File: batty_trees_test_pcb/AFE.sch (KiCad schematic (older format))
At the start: 0 parts

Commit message: Finished off Power section and made up AFE schematic
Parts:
- added D? (x8): B240A-13-F, digikey-footprints:DO-214AC, symbol dk_Diodes-Rectifiers-Single:B240A-13-F
- added J? (x2): JSH_PH_B3B-PH-K, Connector_JST:JST_PH_B3B-PH-K_1x03_P2.00mm_Vertical, symbol Connector:Conn_01x03_Male
- added J? (x2): Header, Connector_PinHeader_2.54mm:PinHeader_1x03_P2.54mm_Vertical, symbol Connector:Conn_01x03_Male
- added JP? (x2): Jumper, Connector_PinHeader_2.54mm:PinHeader_1x02_P2.54mm_Vertical, symbol Device:Jumper_NO_Small
- added R? (x8): 10k, Resistor_SMD:R_0805_2012Metric_Pad1.15x1.40mm_HandSolder, symbol Device:R
- added R? (x8): 100k, Resistor_SMD:R_0805_2012Metric_Pad1.15x1.40mm_HandSolder, symbol Device:R
- added R? (x8): 33k, Resistor_SMD:R_0805_2012Metric_Pad1.15x1.40mm_HandSolder, symbol Device:R
- added R? (x4): 0, Resistor_SMD:R_0805_2012Metric_Pad1.15x1.40mm_HandSolder, symbol Device:R
- added R? (x8): 1k, Resistor_SMD:R_0805_2012Metric_Pad1.15x1.40mm_HandSolder, symbol Device:R
- added R? (x2): 330, Resistor_SMD:R_0805_2012Metric_Pad1.15x1.40mm_HandSolder, symbol Device:R
- added TP? (x6): Test Point, OSU_SIM_BASIC:Keystone_5019, symbol Connector:TestPoint_Alt
- added U? (x12): LMH6611, Package_TO_SOT_SMD:TSOT-23-6, symbol Amplifier_Operational:LMH6611
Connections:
- new net: D?.A, D?.K, R?.1, U?.3 (+) (x4)
- new net: J?.1 (Pin_1), R?.2 (x2)
- new net: J?.3 (Pin_3), R?.2 (x2)
- new net: R?.1, R?.1, U?.3 (+) (x4)
- new net: R?.1, R?.1, U?.4 (-) (x4)
- new net: R?.2, R?.2, R?.2, U?.1 (x4)
- new net: JP?.1, R?.1, TP?.1, U?.1 (x2)
- new net: R?.1, R?.2, R?.2, U?.4 (-) (x2)
- new net: R?.1, R?.1, U?.1 (x2)
- new net: R?.1, R?.2, U?.4 (-) (x2)
- new net +3V3: D?.K, D?.K, D?.K, D?.K, U?.5 (~DISABLE), U?.5 (~DISABLE), U?.5 (~DISABLE), U?.5 (~DISABLE), U?.5 (~DISABLE), U?.5 (~DISABLE), U?.5 (~DISABLE), U?.5 (~DISABLE), U?.5 (~DISABLE), U?.5 (~DISABLE), U?.5 (~DISABLE), U?.5 (~DISABLE), U?.6 (V+), U?.6 (V+), U?.6 (V+), U?.6 (V+), U?.6 (V+), U?.6 (V+), U?.6 (V+), U?.6 (V+), U?.6 (V+), U?.6 (V+), U?.6 (V+), U?.6 (V+)
- new net GND: D?.A, D?.A, D?.A, D?.A, J?.2 (Pin_2), J?.2 (Pin_2), J?.2 (Pin_2), J?.2 (Pin_2), R?.2, R?.2, R?.2, R?.2, U?.2 (V-), U?.2 (V-), U?.2 (V-), U?.2 (V-), U?.2 (V-), U?.2 (V-), U?.2 (V-), U?.2 (V-), U?.2 (V-), U?.2 (V-), U?.2 (V-), U?.2 (V-)
- new net L_VIN_BUFN: J?.3 (Pin_3), R?.1, R?.2, R?.2, U?.1, U?.4 (-)
- new net L_VIN_BUFP: J?.1 (Pin_1), R?.1, R?.2, R?.2, U?.1, U?.4 (-)
- new net R_VIN_BUFN: J?.3 (Pin_3), R?.1, R?.2, R?.2, U?.1, U?.4 (-)
- new net R_VIN_BUFP: J?.1 (Pin_1), R?.1, R?.2, R?.2, U?.1, U?.4 (-)
- new net VMID: R?.2, R?.2, R?.2, R?.2, U?.3 (+), U?.3 (+), U?.3 (+), U?.3 (+)
- new net dd_lin: JP?.2
- new net dd_rin: JP?.2
- new net l_vinn: R?.1, TP?.1
- new net l_vinp: R?.1, TP?.1
- new net r_vinn: R?.1, TP?.1
- new net r_vinp: R?.1, TP?.1
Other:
- note added: "Diff to single ended converter \nwith level shift and gain reduction\nVmid level shift 1/3 gain reduction"
- note added: "Left and right Contact mic input circuitry.\nInpnut clamped at 3.3 and the second stage has gain of\n1/3 to reduce the max input range to 1.2V centered around VMID\nFirst stage buffesrs input with high input impeadance and second stage\nlevel shifts and reduces the gain of the input signal"

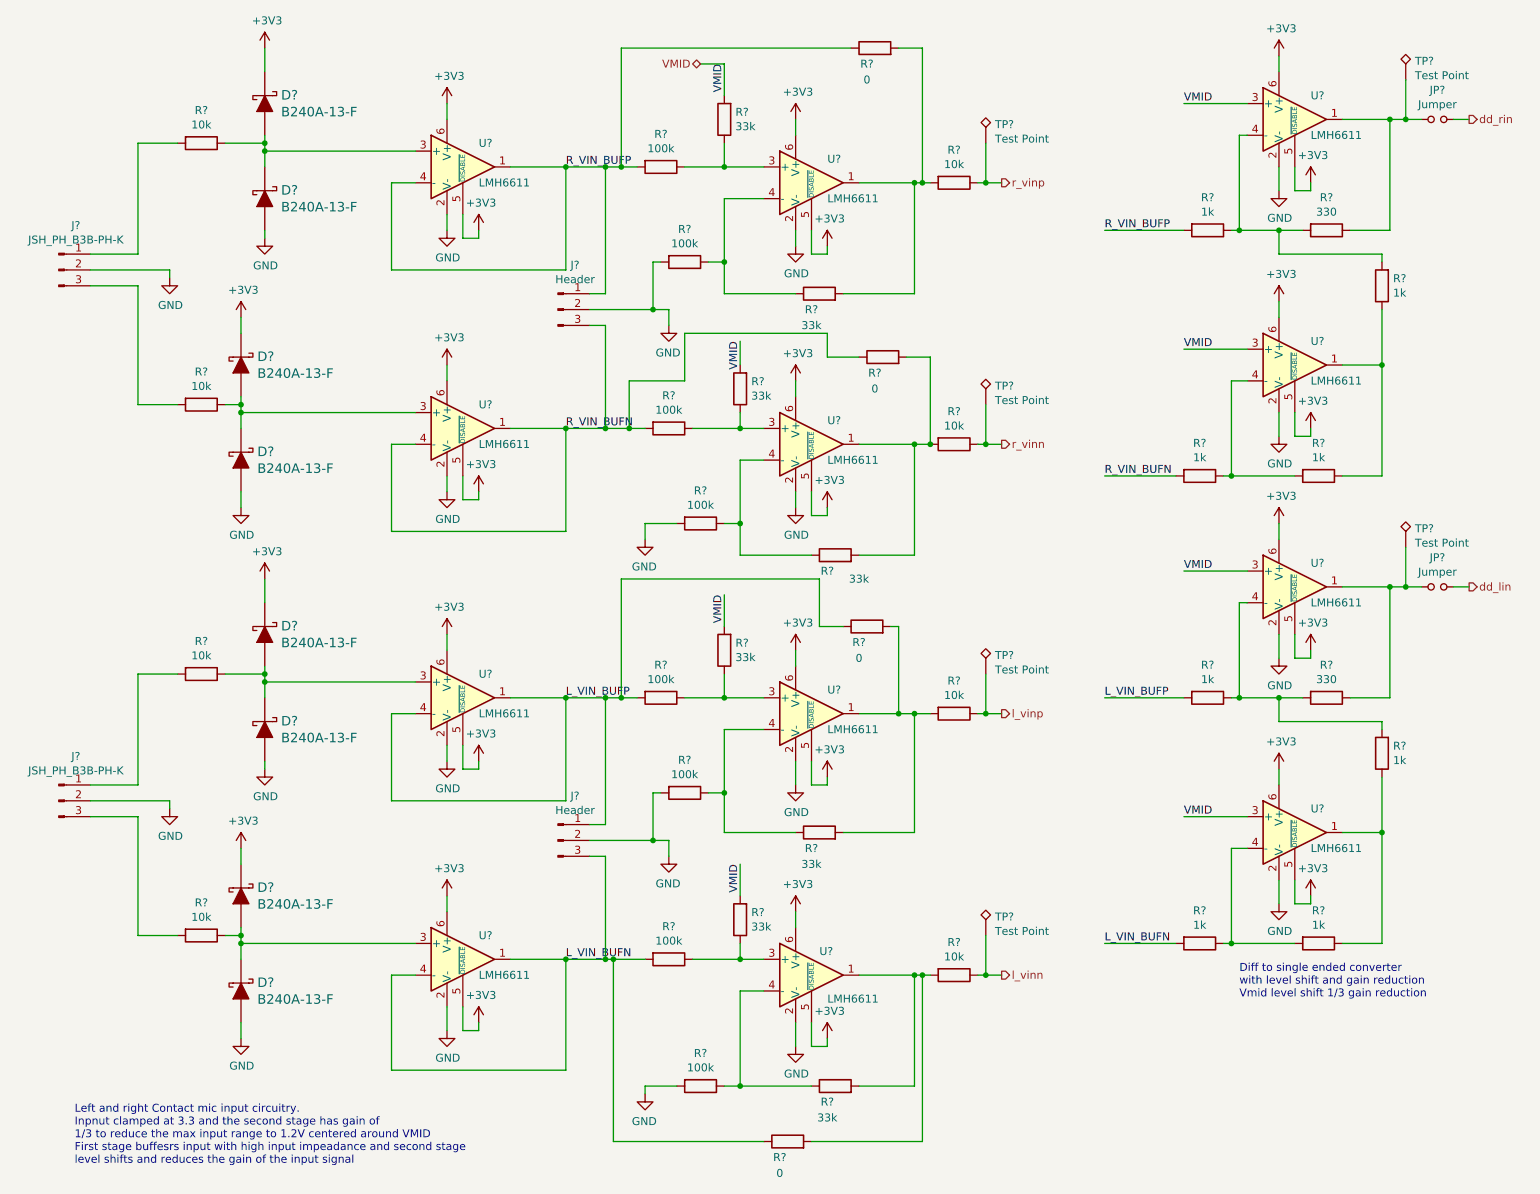
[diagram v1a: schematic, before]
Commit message: wired up chip to fpga on schematic and begininng to do layout
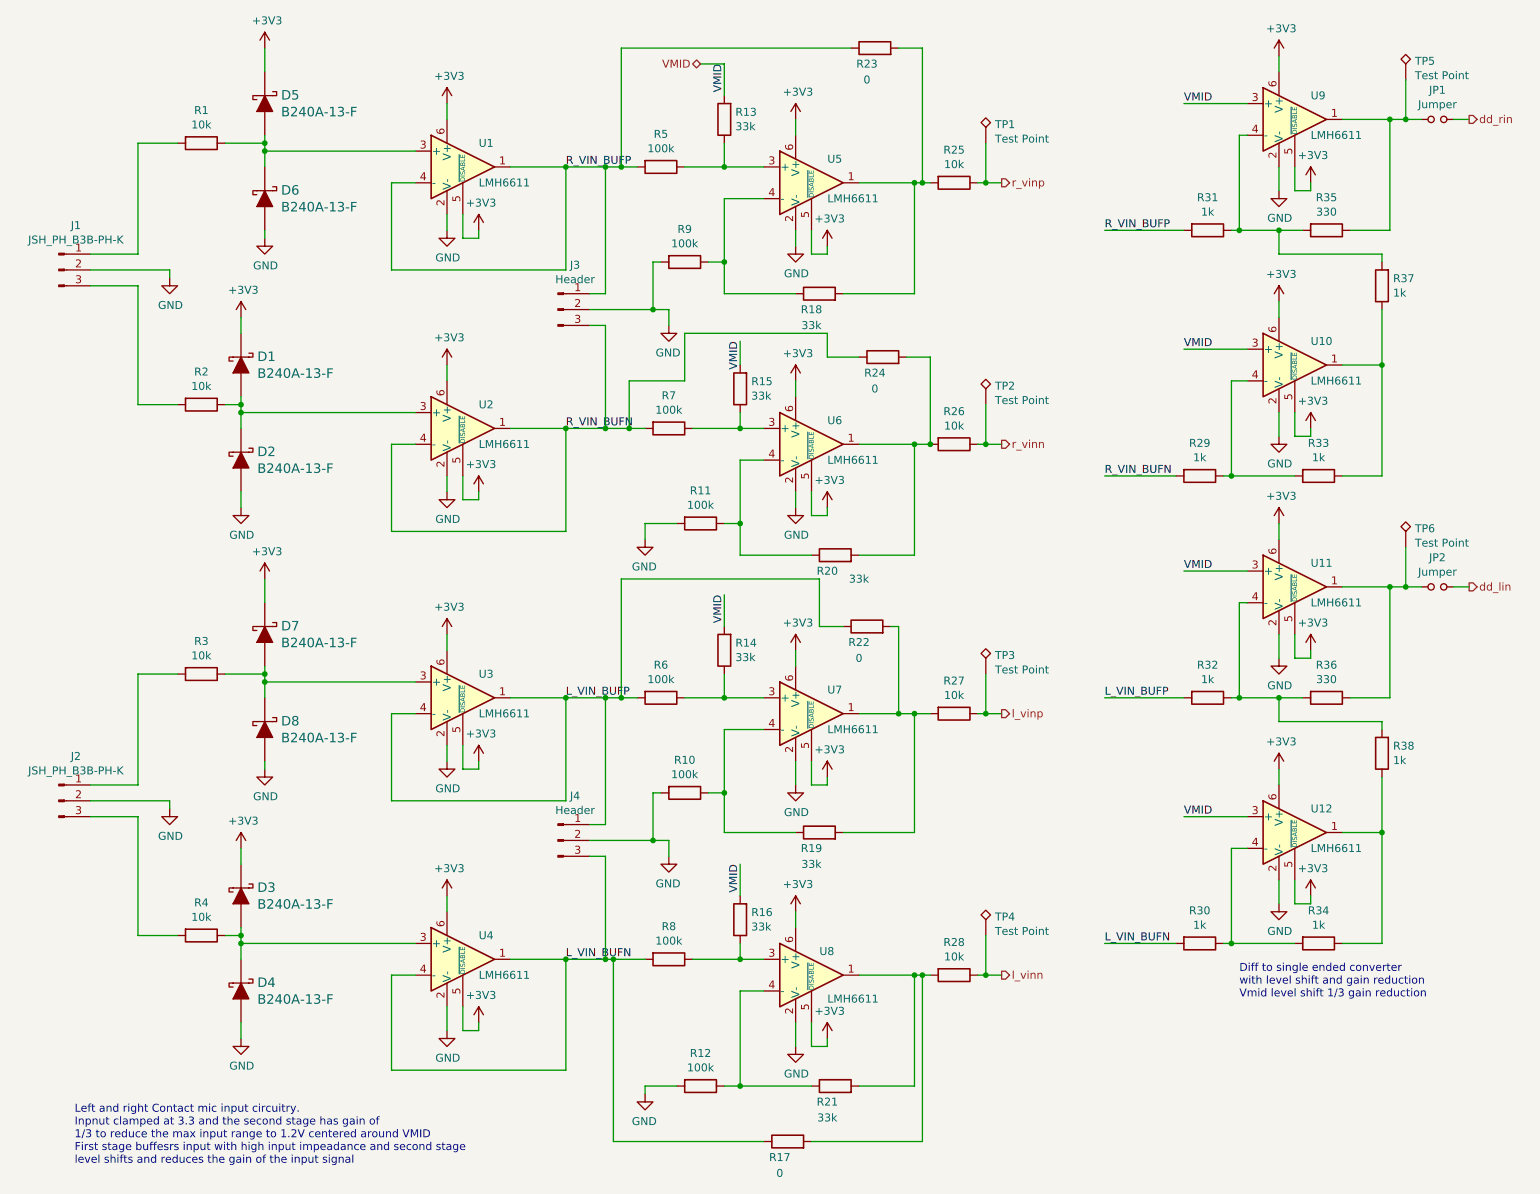
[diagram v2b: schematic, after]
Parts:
- gave numbers to parts that had none: 70

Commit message: more layout work ~90% finished
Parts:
- added C23, C24, C25, C26, C27, C28, C29, C30, C31, C32, C33, C34: 0.1uF, Capacitor_SMD:C_0805_2012Metric_Pad1.15x1.40mm_HandSolder, symbol Device:C_Small
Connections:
- net +3V3: now also C23.1, C24.1, C25.1, C26.1, C27.1, C28.1, C29.1, C30.1, C31.1, C32.1, C33.1, C34.1
- net GND: now also C23.2, C24.2, C25.2, C26.2, C27.2, C28.2, C29.2, C30.2, C31.2, C32.2, C33.2, C34.2
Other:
- note added: "Decap 1 per package"

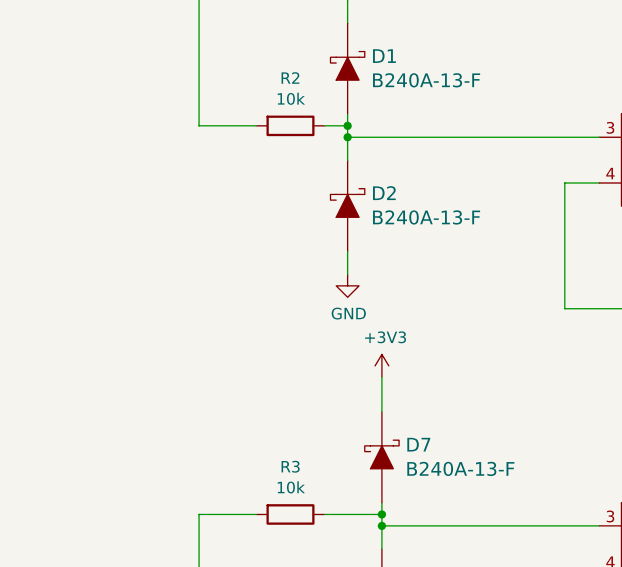
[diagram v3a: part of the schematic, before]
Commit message: all componenets updated with digikey pn bom generated
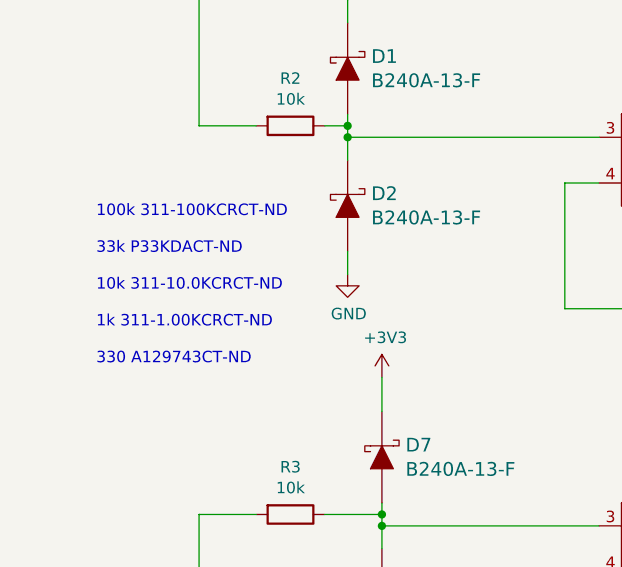
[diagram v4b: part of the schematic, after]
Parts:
- R1, R2, R25, R26, R27, R28, R3, R4: Digi-Key_PN (none) -> 311-10.0KCRCT
- R10, R11, R12, R5, R6, R7, R8, R9: Digi-Key_PN (none) -> 311-100KCRCT-ND
- R13, R14, R15, R16, R18, R19, R20, R21: Digi-Key_PN (none) -> P33KDACT-ND
- R29, R30, R31, R32, R33, R34, R37, R38: Digi-Key_PN (none) -> 311-1.00KCRCT-ND
- R35, R36: Digi-Key_PN (none) -> A129743CT-ND
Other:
- note added: "100k 311-100KCRCT-ND\n\n33k P33KDACT-ND\n\n10k 311-10.0KCRCT-ND\n\n1k 311-1.00KCRCT-ND\n\n330 A129743CT-ND"
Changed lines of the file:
@@
 F 2 "Resistor_SMD:R_0805_2012Metric_Pad1.15x1.40mm_HandSolder" V 1580 1300 50  0001 C CNN
 F 3 "~" H 1650 1300 50  0001 C CNN
+F 4 "311-10.0KCRCT" V 1650 1300 50  0001 C CNN "Digi-Key_PN"
 	1    1650 1300
 	0    1    1    0
@@
 F 2 "Resistor_SMD:R_0805_2012Metric_Pad1.15x1.40mm_HandSolder" V 1580 2950 50  0001 C CNN
 F 3 "~" H 1650 2950 50  0001 C CNN
+F 4 "311-10.0KCRCT" V 1650 2950 50  0001 C CNN "Digi-Key_PN"
 	1    1650 2950
 	0    1    1    0
@@
 F 2 "Resistor_SMD:R_0805_2012Metric_Pad1.15x1.40mm_HandSolder" V 4480 1450 50  0001 C CNN
 F 3 "~" H 4550 1450 50  0001 C CNN
+F 4 "311-100KCRCT-ND" V 4550 1450 50  0001 C CNN "Digi-Key_PN"
 	1    4550 1450
 	0    1    1    0
@@
 F 2 "Resistor_SMD:R_0805_2012Metric_Pad1.15x1.40mm_HandSolder" V 4880 1150 50  0001 C CNN
 F 3 "~" H 4950 1150 50  0001 C CNN
+F 4 "P33KDACT-ND" H 4950 1150 50  0001 C CNN "Digi-Key_PN"
 	1    4950 1150
 	-1   0    0    1
@@
 F 2 "Resistor_SMD:R_0805_2012Metric_Pad1.15x1.40mm_HandSolder" V 4530 3100 50  0001 C CNN
 F 3 "~" H 4600 3100 50  0001 C CNN
+F 4 "311-100KCRCT-ND" V 4600 3100 50  0001 C CNN "Digi-Key_PN"
 	1    4600 3100
 	0    1    1    0
@@
 F 2 "Resistor_SMD:R_0805_2012Metric_Pad1.15x1.40mm_HandSolder" V 4980 2850 50  0001 C CNN
 F 3 "~" H 5050 2850 50  0001 C CNN
+F 4 "P33KDACT-ND" H 5050 2850 50  0001 C CNN "Digi-Key_PN"
 	1    5050 2850
 	-1   0    0    1
@@
 F 2 "Resistor_SMD:R_0805_2012Metric_Pad1.15x1.40mm_HandSolder" V 5480 2250 50  0001 C CNN
 F 3 "~" H 5550 2250 50  0001 C CNN
+F 4 "P33KDACT-ND" V 5550 2250 50  0001 C CNN "Digi-Key_PN"
 	1    5550 2250
 	0    -1   -1   0
@@
 F 2 "Resistor_SMD:R_0805_2012Metric_Pad1.15x1.40mm_HandSolder" V 4630 2050 50  0001 C CNN
 F 3 "~" H 4700 2050 50  0001 C CNN
+F 4 "311-100KCRCT-ND" V 4700 2050 50  0001 C CNN "Digi-Key_PN"
 	1    4700 2050
 	0    1    1    0
@@
 F 2 "Resistor_SMD:R_0805_2012Metric_Pad1.15x1.40mm_HandSolder" V 5580 3900 50  0001 C CNN
 F 3 "~" H 5650 3900 50  0001 C CNN
+F 4 "P33KDACT-ND" V 5650 3900 50  0001 C CNN "Digi-Key_PN"
 	1    5650 3900
 	0    -1   -1   0
@@
 F 2 "Resistor_SMD:R_0805_2012Metric_Pad1.15x1.40mm_HandSolder" V 4730 3700 50  0001 C CNN
 F 3 "~" H 4800 3700 50  0001 C CNN
+F 4 "311-100KCRCT-ND" V 4800 3700 50  0001 C CNN "Digi-Key_PN"
 	1    4800 3700
 	0    1    1    0
@@
 F 2 "Resistor_SMD:R_0805_2012Metric_Pad1.15x1.40mm_HandSolder" V 6330 3200 50  0001 C CNN
 F 3 "~" H 6400 3200 50  0001 C CNN
+F 4 "311-10.0KCRCT" V 6400 3200 50  0001 C CNN "Digi-Key_PN"
 	1    6400 3200
 	0    1    1    0
@@
 F 2 "Resistor_SMD:R_0805_2012Metric_Pad1.15x1.40mm_HandSolder" V 6330 1550 50  0001 C CNN
 F 3 "~" H 6400 1550 50  0001 C CNN
+F 4 "311-10.0KCRCT" V 6400 1550 50  0001 C CNN "Digi-Key_PN"
 	1    6400 1550
 	0    1    1    0
@@
 F 2 "Resistor_SMD:R_0805_2012Metric_Pad1.15x1.40mm_HandSolder" V 1580 4650 50  0001 C CNN
 F 3 "~" H 1650 4650 50  0001 C CNN
+F 4 "311-10.0KCRCT" V 1650 4650 50  0001 C CNN "Digi-Key_PN"
 	1    1650 4650
 	0    1    1    0
@@
 F 2 "Resistor_SMD:R_0805_2012Metric_Pad1.15x1.40mm_HandSolder" V 1580 6300 50  0001 C CNN
 F 3 "~" H 1650 6300 50  0001 C CNN
+F 4 "311-10.0KCRCT" V 1650 6300 50  0001 C CNN "Digi-Key_PN"
 	1    1650 6300
 	0    1    1    0
@@
 F 2 "Resistor_SMD:R_0805_2012Metric_Pad1.15x1.40mm_HandSolder" V 4480 4800 50  0001 C CNN
 F 3 "~" H 4550 4800 50  0001 C CNN
+F 4 "311-100KCRCT-ND" V 4550 4800 50  0001 C CNN "Digi-Key_PN"
 	1    4550 4800
 	0    1    1    0
@@
 F 2 "Resistor_SMD:R_0805_2012Metric_Pad1.15x1.40mm_HandSolder" V 4880 4500 50  0001 C CNN
 F 3 "~" H 4950 4500 50  0001 C CNN
+F 4 "P33KDACT-ND" H 4950 4500 50  0001 C CNN "Digi-Key_PN"
 	1    4950 4500
 	-1   0    0    1
@@
 F 2 "Resistor_SMD:R_0805_2012Metric_Pad1.15x1.40mm_HandSolder" V 4530 6450 50  0001 C CNN
 F 3 "~" H 4600 6450 50  0001 C CNN
+F 4 "311-100KCRCT-ND" V 4600 6450 50  0001 C CNN "Digi-Key_PN"
 	1    4600 6450
 	0    1    1    0
@@
 F 2 "Resistor_SMD:R_0805_2012Metric_Pad1.15x1.40mm_HandSolder" V 4980 6200 50  0001 C CNN
 F 3 "~" H 5050 6200 50  0001 C CNN
+F 4 "P33KDACT-ND" H 5050 6200 50  0001 C CNN "Digi-Key_PN"
 	1    5050 6200
 	-1   0    0    1
@@
 F 2 "Resistor_SMD:R_0805_2012Metric_Pad1.15x1.40mm_HandSolder" V 5480 5650 50  0001 C CNN
 F 3 "~" H 5550 5650 50  0001 C CNN
+F 4 "P33KDACT-ND" V 5550 5650 50  0001 C CNN "Digi-Key_PN"
 	1    5550 5650
 	0    -1   -1   0
@@
 F 2 "Resistor_SMD:R_0805_2012Metric_Pad1.15x1.40mm_HandSolder" V 4630 5400 50  0001 C CNN
 F 3 "~" H 4700 5400 50  0001 C CNN
+F 4 "311-100KCRCT-ND" V 4700 5400 50  0001 C CNN "Digi-Key_PN"
 	1    4700 5400
 	0    1    1    0
@@
 F 2 "Resistor_SMD:R_0805_2012Metric_Pad1.15x1.40mm_HandSolder" V 5580 7250 50  0001 C CNN
 F 3 "~" H 5650 7250 50  0001 C CNN
+F 4 "P33KDACT-ND" V 5650 7250 50  0001 C CNN "Digi-Key_PN"
 	1    5650 7250
 	0    -1   -1   0
@@
 F 2 "Resistor_SMD:R_0805_2012Metric_Pad1.15x1.40mm_HandSolder" V 4730 7250 50  0001 C CNN
 F 3 "~" H 4800 7250 50  0001 C CNN
+F 4 "311-100KCRCT-ND" V 4800 7250 50  0001 C CNN "Digi-Key_PN"
 	1    4800 7250
 	0    1    1    0
@@
 F 2 "Resistor_SMD:R_0805_2012Metric_Pad1.15x1.40mm_HandSolder" V 6330 6550 50  0001 C CNN
 F 3 "~" H 6400 6550 50  0001 C CNN
+F 4 "311-10.0KCRCT" V 6400 6550 50  0001 C CNN "Digi-Key_PN"
 	1    6400 6550
 	0    1    1    0
@@
 F 2 "Resistor_SMD:R_0805_2012Metric_Pad1.15x1.40mm_HandSolder" V 6330 4900 50  0001 C CNN
 F 3 "~" H 6400 4900 50  0001 C CNN
+F 4 "311-10.0KCRCT" V 6400 4900 50  0001 C CNN "Digi-Key_PN"
 	1    6400 4900
 	0    1    1    0
@@
 F 2 "Resistor_SMD:R_0805_2012Metric_Pad1.15x1.40mm_HandSolder" V 8630 3400 50  0001 C CNN
 F 3 "~" H 8700 3400 50  0001 C CNN
+F 4 "311-1.00KCRCT-ND" V 8700 3400 50  0001 C CNN "Digi-Key_PN"
 	1    8700 3400
 	0    1    1    0
@@
 F 2 "Resistor_SMD:R_0805_2012Metric_Pad1.15x1.40mm_HandSolder" V 7880 3400 50  0001 C CNN
 F 3 "~" H 7950 3400 50  0001 C CNN
+F 4 "311-1.00KCRCT-ND" V 7950 3400 50  0001 C CNN "Digi-Key_PN"
 	1    7950 3400
 	0    1    1    0
@@
 F 2 "Resistor_SMD:R_0805_2012Metric_Pad1.15x1.40mm_HandSolder" V 9030 2200 50  0001 C CNN
 F 3 "~" H 9100 2200 50  0001 C CNN
+F 4 "311-1.00KCRCT-ND" H 9100 2200 50  0001 C CNN "Digi-Key_PN"
 	1    9100 2200
 	-1   0    0    1
@@
 F 2 "Resistor_SMD:R_0805_2012Metric_Pad1.15x1.40mm_HandSolder" V 8680 1850 50  0001 C CNN
 F 3 "~" H 8750 1850 50  0001 C CNN
+F 4 "A129743CT-ND" V 8750 1850 50  0001 C CNN "Digi-Key_PN"
 	1    8750 1850
 	0    1    1    0
@@
 F 2 "Resistor_SMD:R_0805_2012Metric_Pad1.15x1.40mm_HandSolder" V 7930 1850 50  0001 C CNN
 F 3 "~" H 8000 1850 50  0001 C CNN
+F 4 "311-1.00KCRCT-ND" V 8000 1850 50  0001 C CNN "Digi-Key_PN"
 	1    8000 1850
 	0    1    1    0
@@
 F 2 "Resistor_SMD:R_0805_2012Metric_Pad1.15x1.40mm_HandSolder" V 8630 6350 50  0001 C CNN
 F 3 "~" H 8700 6350 50  0001 C CNN
+F 4 "311-1.00KCRCT-ND" V 8700 6350 50  0001 C CNN "Digi-Key_PN"
 	1    8700 6350
 	0    1    1    0
@@
 F 2 "Resistor_SMD:R_0805_2012Metric_Pad1.15x1.40mm_HandSolder" V 7880 6350 50  0001 C CNN
 F 3 "~" H 7950 6350 50  0001 C CNN
+F 4 "311-1.00KCRCT-ND" V 7950 6350 50  0001 C CNN "Digi-Key_PN"
 	1    7950 6350
 	0    1    1    0
@@
 F 2 "Resistor_SMD:R_0805_2012Metric_Pad1.15x1.40mm_HandSolder" V 9030 5150 50  0001 C CNN
 F 3 "~" H 9100 5150 50  0001 C CNN
+F 4 "311-1.00KCRCT-ND" H 9100 5150 50  0001 C CNN "Digi-Key_PN"
 	1    9100 5150
 	-1   0    0    1
@@
 F 2 "Resistor_SMD:R_0805_2012Metric_Pad1.15x1.40mm_HandSolder" V 8680 4800 50  0001 C CNN
 F 3 "~" H 8750 4800 50  0001 C CNN
+F 4 "A129743CT-ND" V 8750 4800 50  0001 C CNN "Digi-Key_PN"
 	1    8750 4800
 	0    1    1    0
@@
 F 2 "Resistor_SMD:R_0805_2012Metric_Pad1.15x1.40mm_HandSolder" V 7930 4800 50  0001 C CNN
 F 3 "~" H 8000 4800 50  0001 C CNN
+F 4 "311-1.00KCRCT-ND" V 8000 4800 50  0001 C CNN "Digi-Key_PN"
 	1    8000 4800
 	0    1    1    0
@@
 Text Notes 7100 1300 0    50   ~ 0
 Decap 1 per package
+Text Notes 800  4000 0    50   ~ 0
+100k 311-100KCRCT-ND\n\n33k P33KDACT-ND\n\n10k 311-10.0KCRCT-ND\n\n1k 311-1.00KCRCT-ND\n\n330 A129743CT-ND
 $EndSCHEMATC
